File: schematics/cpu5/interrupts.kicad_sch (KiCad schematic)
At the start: 16 parts, among them U83 74LS08, U84 74LS32, U85 74LS32, U86 74LS04, U87 74LS02, U88 74LS02, U89 74LS08, U90 74LS32, U91 74LS541, U92 74LS32

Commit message: start faults
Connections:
- net INT1 is gone; now on net MMU_FAULT: IntBoardConn2.2 (Pin_2), U87.12 (B4)
- net GND: now also U92.13 (B4)
- net FAULT: now reaches U92.11 (Y4)
- net MMU_FAULT: now reaches U92.12 (A4)
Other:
- moved on the sheet: U92D

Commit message: faults seem to work
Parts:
- added U127: 74LS08, Package_DIP:DIP-14_W7.62mm, symbol 7400_ice:74LS08
- added U128, U129: 74LS74, Package_DIP:DIP-14_W7.62mm, symbol 7400_ice:74LS74
- added U130: 74LS04, Package_DIP:DIP-14_W7.62mm, symbol 7400_ice:74LS04
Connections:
- net INT3 is gone; now on net DBG_PRE_INT3: IntBoardConn2.4 (Pin_4), U89.10 (B3)
- net +5V: now also U127.14 (VCC), U128.10 (nS2), U128.12 (D2), U128.14 (VCC), U128.2 (D1), U128.4 (nS1), U129.14 (VCC), U129.2 (D1), U129.4 (nS1), U130.14 (VCC)
- net DBG_PRE_INT1: now also U83.2 (B1), U84.10 (B3), U128.9 (Q2); no longer ML7.3 (D1), U83.3 (Y1)
- net DBG_PRE_INT2: now also U84.13 (B4), U89.5 (B2), U129.5 (Q1); no longer ML7.4 (D2), U89.6 (Y2)
- net DBG_PRE_INT3: no longer ML7.5 (D3), U89.8 (Y3)
- net GND: now also U127.7 (GND), U128.7 (GND), U129.7 (GND), U130.7 (GND)
- net INT0: now also U128.3 (Clk1); no longer U87.6 (B2)
- net INT2: now also U129.3 (Clk1); no longer U88.6 (B2)
- net MMU_FAULT: now also U128.11 (Clk2); no longer U87.12 (B4)
- net at U85.3 (Y1): now also U130.3 (A1); no longer U87.8 (A3)
- net DBG_PRE_INT0: now reaches ML7.2 (D0), U84.9 (A3), U86.3 (A1)
- net DBG_PRE_INT0: now also U128.5 (Q1); no longer U87.1 (Y1), U87.5 (A2)
- net at U88.2 (A1): no longer U84.6 (Y2)
- net at U88.3 (B1): no longer U88.4 (Y2)
- net at U87.4 (Y2): no longer U87.3 (B1)
- net at U84.3 (Y1): now also U130.1 (A0); no longer U87.2 (A1)
- net at U87.9 (B3): no longer U87.13 (Y4)
- new net: U128.1 (nR1), U130.2 (Y0)
- new net: U129.1 (nR1), U130.6 (Y2)
- new net: ML7.3 (D1), U83.3 (Y1)
- new net: ML7.5 (D3), U89.8 (Y3)
- new net: U130.5 (A2), U84.6 (Y2)
- new net: U128.13 (nR2), U130.4 (Y1)
- new net: ML7.4 (D2), U89.6 (Y2)
- now unconnected: U87.10 (Y3), U87.11 (A4), U88.1 (Y1), U88.5 (A2)
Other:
- moved on the sheet: U83B, U83C, U83D, U84A, U84B, U85A, U87A, U87B, U87C, U87D, U88A, U88B

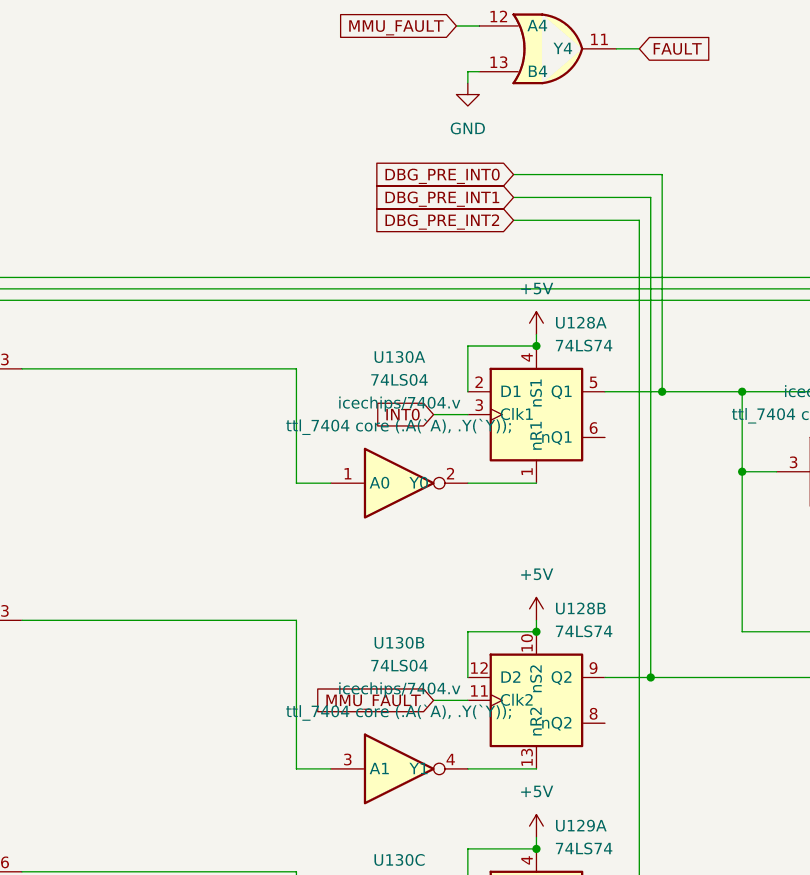
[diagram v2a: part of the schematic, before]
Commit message: Page faults work
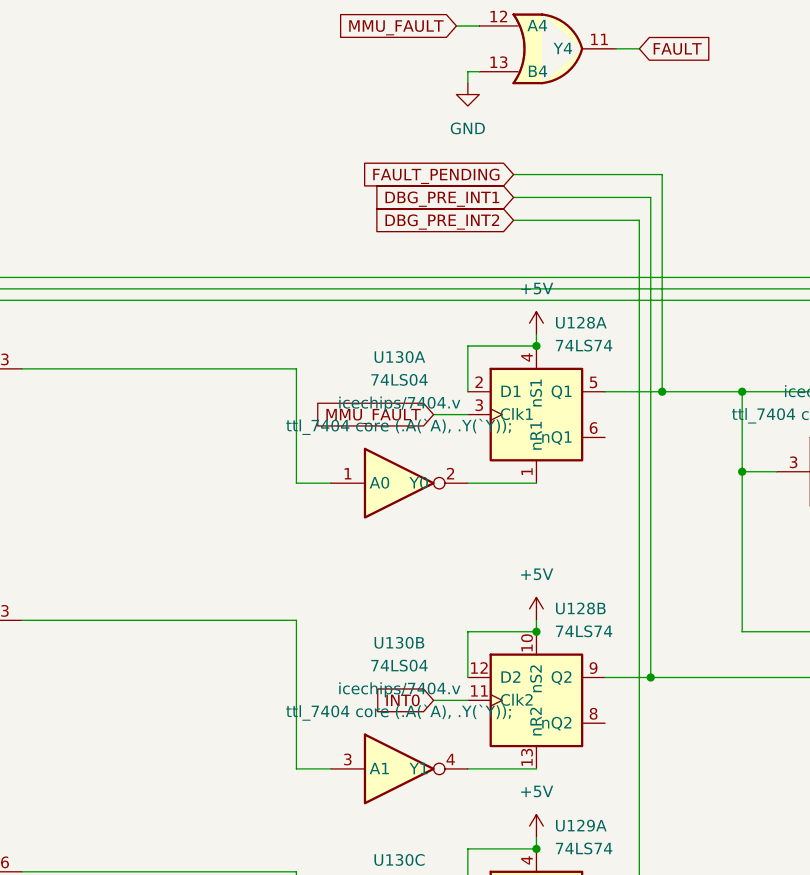
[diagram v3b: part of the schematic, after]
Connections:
- net INT0: now also U128.11 (Clk2); no longer U128.3 (Clk1)
- net MMU_FAULT: now also U128.3 (Clk1); no longer U128.11 (Clk2)
- net DBG_PRE_INT0 renamed FAULT_PENDING

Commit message: perf experiments
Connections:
- net DBG_PRE_INT3: no longer IntBoardConn2.4 (Pin_4), U89.10 (B3)
- new net INT3: IntBoardConn2.4 (Pin_4), U89.10 (B3)
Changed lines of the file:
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@@
-    (stroke (width 0) (type default) (color 0 0 0 0))
-  )
-  (wire (pts (xy 232.41 193.04) (xy 232.41 199.39))
     (stroke (width 0) (type default) (color 0 0 0 0))
   )
@@
   )
   (wire (pts (xy 198.12 146.05) (xy 208.28 146.05))
-    (stroke (width 0) (type default) (color 0 0 0 0))
-  )
-  (wire (pts (xy 228.6 199.39) (xy 232.41 199.39))
     (stroke (width 0) (type default) (color 0 0 0 0))
   )
@@
       (effects (font (size 1.27 1.27)) (justify right) hide)
     )
-  )
-  (global_label "DBG_PRE_INT3" (shape input) (at 228.6 199.39 180) (fields_autoplaced)
-    (effects (font (size 1.27 1.27)) (justify right))
-    (property "Intersheet References" "${INTERSHEET_REFS}" (id 0) (at 212.6402 199.3106 0)
-      (effects (font (size 1.27 1.27)) (justify right) hide)
-    )
